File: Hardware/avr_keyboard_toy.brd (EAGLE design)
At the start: 22.9 x 47.6 mm, 16 parts, among them CN1 MISC, J1 TFT, J2 I2C, J3 MISC2, SW1 SPST_TACT-EVQQ2, U1 ATMEGA328P-AU

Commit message: Slight changes to the board
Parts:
- moved SP1 1.90 mm to (27.9, 15.2)
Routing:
- net VCC: track 90.2 -> 88.0 mm
- net PIEZO: track 12.1 -> 10.2 mm
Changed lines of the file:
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@@
 <text x="36.83" y="6.985" size="1.016" layer="22" font="vector" rot="MR0">AVR Keyboard Toy
 Board revision B</text>
-<text x="27.94" y="17.78" size="1.27" layer="22" font="vector" rot="MR0">Petezah</text>
+<text x="26.67" y="17.78" size="1.27" layer="22" font="vector" rot="MR0">Petezah</text>
 <text x="31.4325" y="3.81" size="0.6096" layer="22" font="vector" rot="MR0">(c) 2016 Peter Dunshee
 @Petezah
@@
 </element>
 <element name="R3" library="adafruit" package="R1206" value="10k" x="20.32" y="3.81" rot="R90"/>
-<element name="SP1" library="adafruit" package="PS12" value="SPEAKER/PS12" x="27.94" y="13.335" smashed="yes" rot="R270">
-<attribute name="NAME" x="31.115" y="17.145" size="1.27" layer="25" ratio="10" rot="R270"/>
-<attribute name="VALUE" x="24.13" y="17.2212" size="1.27" layer="27" ratio="10" rot="R270"/>
+<element name="SP1" library="adafruit" package="PS12" value="SPEAKER/PS12" x="27.94" y="15.24" smashed="yes" rot="R270">
+<attribute name="NAME" x="31.115" y="19.05" size="1.27" layer="25" ratio="10" rot="R270"/>
+<attribute name="VALUE" x="24.13" y="19.1262" size="1.27" layer="27" ratio="10" rot="R270"/>
 </element>
 <element name="UART" library="SparkFun-Connectors" package="1X04" value="" x="20.32" y="8.89" smashed="yes" rot="MR90">
@@
 <wire x1="36.83" y1="17.78" x2="32.385" y2="17.78" width="0.2032" layer="16"/>
 <wire x1="32.385" y1="17.78" x2="31.115" y2="16.51" width="0.2032" layer="16"/>
-<wire x1="31.115" y1="16.51" x2="31.115" y2="14.9225" width="0.2032" layer="1"/>
-<wire x1="31.115" y1="14.9225" x2="29.5275" y2="13.335" width="0.2032" layer="1"/>
-<wire x1="29.5275" y1="13.335" x2="23.495" y2="13.335" width="0.2032" layer="1"/>
-<wire x1="23.495" y1="13.335" x2="20.32" y2="16.51" width="0.2032" layer="1"/>
+<wire x1="31.115" y1="16.51" x2="29.845" y2="14.9225" width="0.2032" layer="1"/>
+<wire x1="29.845" y1="14.9225" x2="22.225" y2="14.9225" width="0.2032" layer="1"/>
+<wire x1="22.225" y1="14.9225" x2="20.32" y2="16.51" width="0.2032" layer="1"/>
 <wire x1="26.509540625" y1="24.18625" x2="26.72625" y2="24.18625" width="0.2032" layer="1"/>
 <wire x1="26.72625" y1="24.18625" x2="28.8925" y2="26.3525" width="0.2032" layer="1"/>
@@
 <contactref element="U1" pad="13"/>
 <contactref element="SP1" pad="P$1"/>
-<wire x1="27.94" y1="15.835" x2="27.94" y2="17.78" width="0.2032" layer="1"/>
+<wire x1="27.94" y1="17.74" x2="27.94" y2="17.78" width="0.2032" layer="1"/>
 <wire x1="27.94" y1="17.78" x2="33.02" y2="22.86" width="0.2032" layer="1"/>
 <wire x1="33.02" y1="22.86" x2="33.02" y2="24.06973125" width="0.2032" layer="1"/>

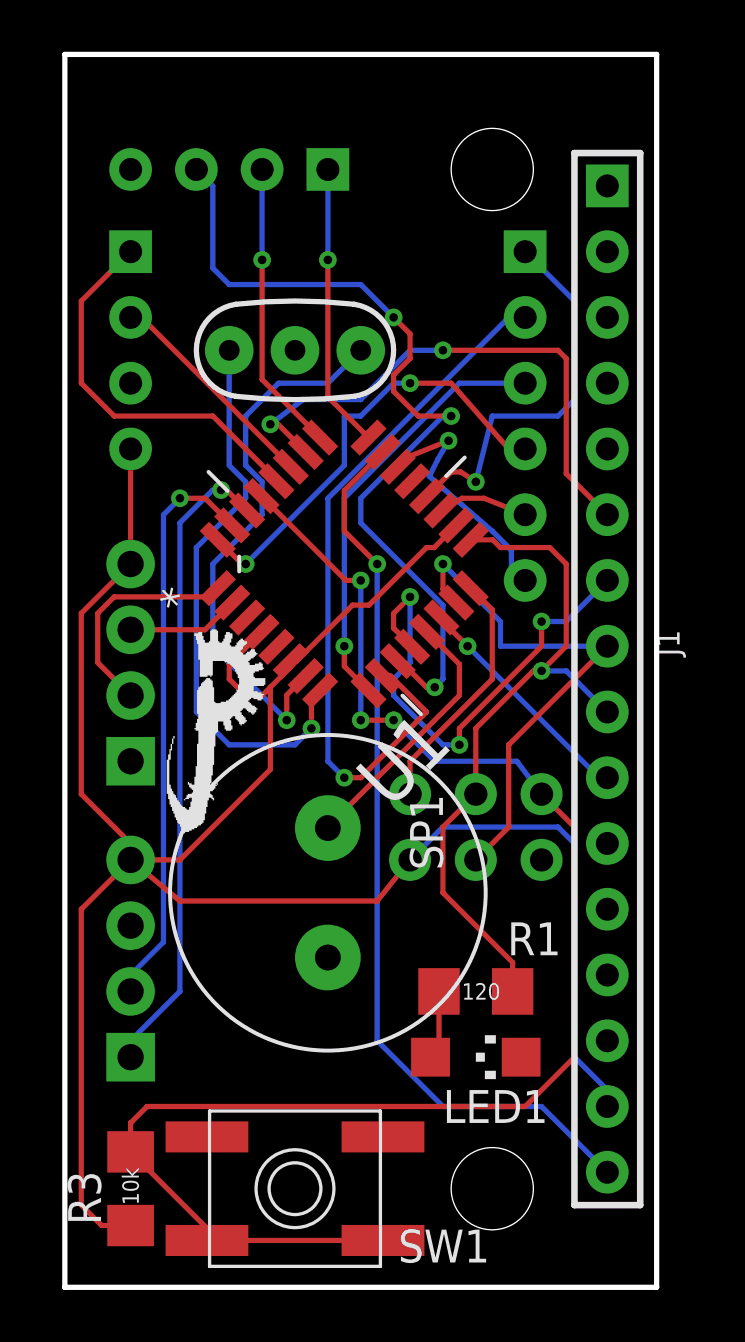
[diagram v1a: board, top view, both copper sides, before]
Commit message: Tweaking the silkscreen a bit
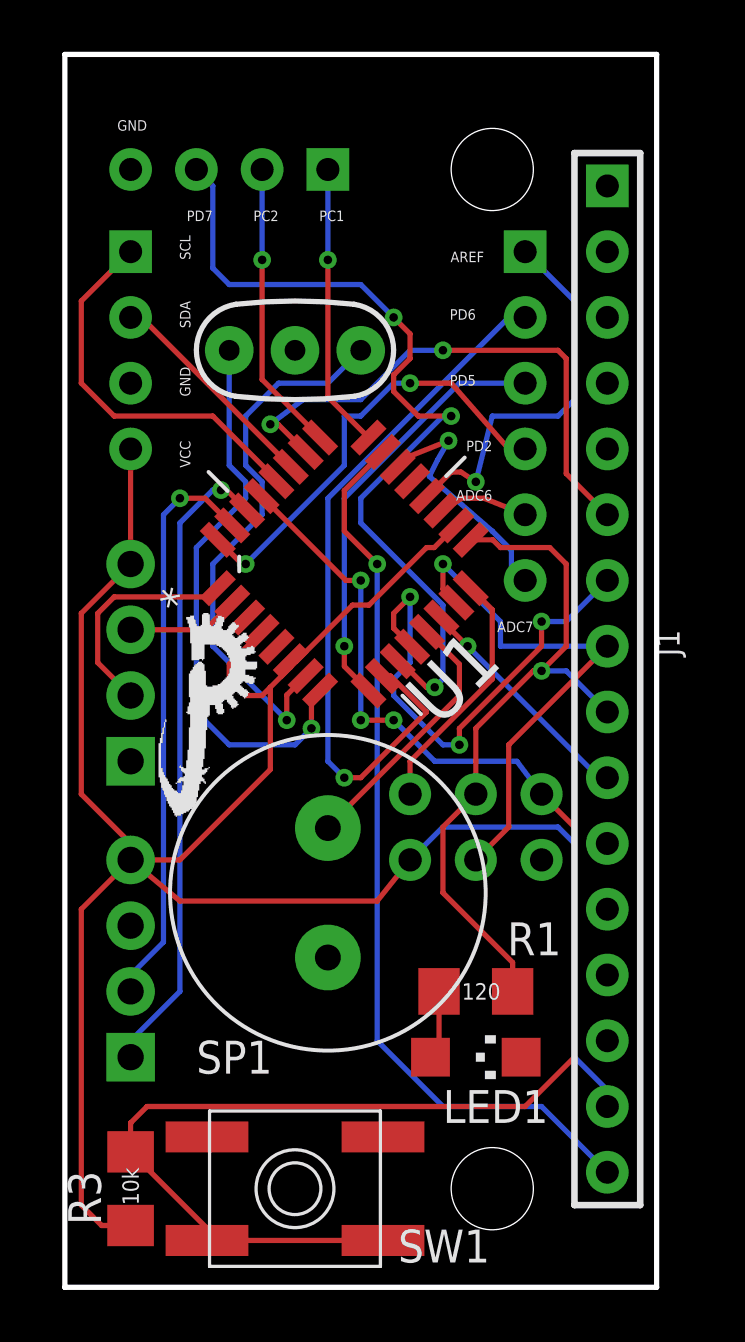
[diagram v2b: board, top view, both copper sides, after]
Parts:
- moved U$1 0.71 mm to (21.3, 18.1)
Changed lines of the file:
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@@
 <text x="18.7325" y="28.575" size="0.4064" layer="22" font="vector" rot="MR270">VCC</text>
 <text x="18.7325" y="20.955" size="0.4064" layer="22" font="vector" rot="MR270">GND</text>
-<text x="22.225" y="32.7025" size="0.4064" layer="22" font="vector" rot="MR270">VCC</text>
-<text x="22.225" y="35.56" size="0.4064" layer="22" font="vector" rot="MR270">GND</text>
-<text x="22.225" y="38.1" size="0.4064" layer="22" font="vector" rot="MR270">SDA</text>
-<text x="22.225" y="40.64" size="0.4064" layer="22" font="vector" rot="MR270">SCL</text>
-<text x="33.02" y="31.4325" size="0.4064" layer="22" font="vector" rot="MR180">PD2</text>
-<text x="33.02" y="35.2425" size="0.4064" layer="22" font="vector" rot="MR180">PD5</text>
-<text x="33.02" y="37.7825" size="0.4064" layer="22" font="vector" rot="MR180">PD6</text>
-<text x="32.7025" y="40.005" size="0.4064" layer="22" font="vector" rot="MR180">AREF</text>
-<text x="32.7025" y="29.845" size="0.4064" layer="22" font="vector" rot="MR180">ADC6</text>
-<text x="32.7025" y="27.6225" size="0.4064" layer="22" font="vector" rot="MR180">ADC7</text>
-<text x="27.305" y="41.5925" size="0.4064" layer="22" font="vector" rot="MR180">PC1</text>
-<text x="24.765" y="41.5925" size="0.4064" layer="22" font="vector" rot="MR180">PC2</text>
-<text x="22.225" y="41.5925" size="0.4064" layer="22" font="vector" rot="MR180">PD7</text>
-<text x="19.685" y="45.085" size="0.4064" layer="22" font="vector" rot="MR180">GND</text>
+<text x="22.225" y="32.7025" size="0.4064" layer="21" font="vector" rot="R270">VCC</text>
+<text x="22.225" y="35.56" size="0.4064" layer="21" font="vector" rot="R270">GND</text>
+<text x="22.225" y="38.1" size="0.4064" layer="21" font="vector" rot="R270">SDA</text>
+<text x="22.225" y="40.64" size="0.4064" layer="21" font="vector" rot="R270">SCL</text>
+<text x="34.29" y="32.7025" size="0.4064" layer="21" font="vector" rot="R180">PD2</text>
+<text x="33.655" y="35.2425" size="0.4064" layer="21" font="vector" rot="R180">PD5</text>
+<text x="33.655" y="37.7825" size="0.4064" layer="21" font="vector" rot="R180">PD6</text>
+<text x="33.9725" y="40.005" size="0.4064" layer="21" font="vector" rot="R180">AREF</text>
+<text x="34.29" y="30.7975" size="0.4064" layer="21" font="vector" rot="R180">ADC6</text>
+<text x="35.8775" y="25.7175" size="0.4064" layer="21" font="vector" rot="R180">ADC7</text>
+<text x="28.575" y="41.5925" size="0.4064" layer="21" font="vector" rot="R180">PC1</text>
+<text x="26.035" y="41.5925" size="0.4064" layer="21" font="vector" rot="R180">PC2</text>
+<text x="23.495" y="41.5925" size="0.4064" layer="21" font="vector" rot="R180">PD7</text>
+<text x="20.955" y="45.085" size="0.4064" layer="21" font="vector" rot="R180">GND</text>
 <wire x1="17.78" y1="47.625" x2="40.64" y2="47.625" width="0.2032" layer="20"/>
 <wire x1="40.64" y1="47.625" x2="40.64" y2="0" width="0.2032" layer="20"/>
@@
 <element name="R3" library="adafruit" package="R1206" value="10k" x="20.32" y="3.81" rot="R90"/>
 <element name="SP1" library="adafruit" package="PS12" value="SPEAKER/PS12" x="27.94" y="15.24" smashed="yes" rot="R270">
-<attribute name="NAME" x="31.115" y="19.05" size="1.27" layer="25" ratio="10" rot="R270"/>
+<attribute name="NAME" x="22.86" y="8.255" size="1.27" layer="25" ratio="10"/>
 <attribute name="VALUE" x="24.13" y="19.1262" size="1.27" layer="27" ratio="10" rot="R270"/>
 </element>
@@
 <element name="XTAL1" library="SparkFun-FreqCtrl" package="RESONATOR-PTH" value="" x="26.67" y="36.195" rot="R180"/>
 <element name="U$2" library="petezah" package="LOGO_SM" value="" x="31.115" y="18.415" rot="MR0"/>
-<element name="U$1" library="petezah" package="LOGO_TINY" value="" x="21.59" y="17.4625"/>
-<element name="U1" library="Atmel_By_element14_Batch_1-00" package="QFP80P900X900X120-32N" value="ATMEGA328P-AU" x="28.575" y="27.94" rot="R45">
+<element name="U$1" library="petezah" package="LOGO_TINY" value="" x="21.2725" y="18.0975"/>
+<element name="U1" library="Atmel_By_element14_Batch_1-00" package="QFP80P900X900X120-32N" value="ATMEGA328P-AU" x="28.575" y="27.94" smashed="yes" rot="R45">
 <attribute name="PACKAGE" value="TQFP-32" x="28.575" y="27.94" size="1.778" layer="27" rot="R45" display="off"/>
 <attribute name="OC_NEWARK" value="14R4631" x="28.575" y="27.94" size="1.778" layer="27" rot="R45" display="off"/>
@@
 <attribute name="OC_FARNELL" value="1715486" x="28.575" y="27.94" size="1.778" layer="27" rot="R45" display="off"/>
 <attribute name="SUPPLIER" value="Atmel" x="28.575" y="27.94" size="1.778" layer="27" rot="R45" display="off"/>
+<attribute name="NAME" x="32.240128125" y="21.595928125" size="2.0828" layer="25" ratio="10" rot="SR45"/>
+<attribute name="VALUE" x="20.49276875" y="31.13696875" size="2.0828" layer="27" ratio="10" rot="SR45"/>
 </element>
 <element name="J1" library="Seeed-OPL-Connector" package="H16-2.54" value="TFT" x="38.735" y="23.495" rot="R180">
